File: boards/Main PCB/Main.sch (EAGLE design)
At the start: 87 parts, among them CN1 MINIB, CN2 MINIB, IC1 FT232RL, IC2 FT232RL, J1 3_PIN_JST-XH, J2 2_PIN_JST-XH, Q4 BSS138, Q5 BSS138, Q6 BSS138, Q7 BSS138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

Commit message: Fixed board to adhere to DRC's and fixed schematic to adhere to ERC's
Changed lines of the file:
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@@
 <part name="+3V9" library="supply1" library_urn="urn:adsk.eagle:library:371" deviceset="+3V3" device=""/>
 <part name="U4" library="TXS0104EDR" deviceset="TXS0104EDR" device=""/>
-<part name="+3V10" library="supply1" library_urn="urn:adsk.eagle:library:371" deviceset="+3V3" device=""/>
-<part name="P+6" library="supply1" library_urn="urn:adsk.eagle:library:371" deviceset="+5V" device=""/>
 <part name="GND32" library="supply1" library_urn="urn:adsk.eagle:library:371" deviceset="GND" device=""/>
 </parts>
@@
 <attribute name="NAME" x="431.35583125" y="94.6727" size="2.08746875" layer="95" ratio="10" rot="SMR180"/>
 <attribute name="VALUE" x="434.13266875" y="143.4777" size="2.08593125" layer="96" ratio="10" rot="SMR180"/>
-</instance>
-<instance part="+3V10" gate="G$1" x="411.48" y="104.14" smashed="yes">
-<attribute name="VALUE" x="408.94" y="99.06" size="1.778" layer="96" rot="R90"/>
-</instance>
-<instance part="P+6" gate="1" x="406.4" y="106.68" smashed="yes">
-<attribute name="VALUE" x="403.86" y="101.6" size="1.778" layer="96" rot="R90"/>
 </instance>
 <instance part="GND32" gate="1" x="414.02" y="132.08" smashed="yes">
@@
 <segment>
 <pinref part="U4" gate="A" pin="VCCA"/>
-<pinref part="+3V10" gate="G$1" pin="+3V3"/>
-<wire x1="419.1" y1="101.6" x2="411.48" y2="101.6" width="0.1524" layer="91"/>
+<wire x1="419.1" y1="101.6" x2="406.4" y2="101.6" width="0.1524" layer="91"/>
+<label x="406.4" y="101.6" size="1.778" layer="95" rot="R180"/>
 </segment>
 </net>
@@
 </segment>
 <segment>
+<pinref part="X1" gate="-5" pin="S"/>
+<label x="472.44" y="111.76" size="1.778" layer="95" rot="R90" xref="yes"/>
+<wire x1="472.44" y1="101.6" x2="472.44" y2="111.76" width="0.1524" layer="91"/>
+</segment>
+<segment>
 <pinref part="U4" gate="A" pin="VCCB"/>
-<pinref part="P+6" gate="1" pin="+5V"/>
 <wire x1="419.1" y1="104.14" x2="416.56" y2="104.14" width="0.1524" layer="91"/>
 <pinref part="U4" gate="A" pin="OE"/>
-<wire x1="416.56" y1="104.14" x2="406.4" y2="104.14" width="0.1524" layer="91"/>
+<wire x1="416.56" y1="104.14" x2="414.02" y2="104.14" width="0.1524" layer="91"/>
 <wire x1="419.1" y1="121.92" x2="416.56" y2="121.92" width="0.1524" layer="91"/>
 <wire x1="416.56" y1="121.92" x2="416.56" y2="104.14" width="0.1524" layer="91"/>
 <junction x="416.56" y="104.14"/>
-</segment>
-<segment>
-<pinref part="X1" gate="-5" pin="S"/>
-<label x="472.44" y="111.76" size="1.778" layer="95" rot="R90" xref="yes"/>
-<wire x1="472.44" y1="101.6" x2="472.44" y2="111.76" width="0.1524" layer="91"/>
+<label x="414.02" y="104.14" size="1.778" layer="95" rot="R180"/>
 </segment>
 </net>
@@
 <net name="N$46" class="0">
 <segment>
-<wire x1="114.3" y1="152.4" x2="114.3" y2="137.16" width="0.1524" layer="91"/>
+<wire x1="114.3" y1="144.78" x2="114.3" y2="137.16" width="0.1524" layer="91"/>
 <pinref part="U2" gate="G$1" pin="PA4/SPI1_NSS/TIM14_CH1/USART2_CK/USB_NOE/ADC_IN4"/>
 <wire x1="114.3" y1="137.16" x2="172.72" y2="137.16" width="0.1524" layer="91"/>
@@
 <pinref part="Q4" gate="G$1" pin="S"/>
 <wire x1="20.32" y1="154.94" x2="35.56" y2="154.94" width="0.1524" layer="91"/>
-<wire x1="114.3" y1="152.4" x2="35.56" y2="152.4" width="0.1524" layer="91"/>
-<wire x1="35.56" y1="152.4" x2="35.56" y2="154.94" width="0.1524" layer="91"/>
+<wire x1="114.3" y1="144.78" x2="35.56" y2="144.78" width="0.1524" layer="91"/>
+<wire x1="35.56" y1="144.78" x2="35.56" y2="154.94" width="0.1524" layer="91"/>
 <junction x="35.56" y="154.94"/>
 </segment>
@@
 <net name="N$50" class="0">
 <segment>
-<pinref part="Q8" gate="G$1" pin="S"/>
-<pinref part="R30" gate="G$1" pin="1"/>
-<wire x1="20.32" y1="203.2" x2="35.56" y2="203.2" width="0.1524" layer="91"/>
-<junction x="35.56" y="203.2"/>
-<wire x1="35.56" y1="203.2" x2="119.38" y2="203.2" width="0.1524" layer="91"/>
-<wire x1="119.38" y1="203.2" x2="119.38" y2="147.32" width="0.1524" layer="91"/>
+<wire x1="119.38" y1="182.88" x2="119.38" y2="147.32" width="0.1524" layer="91"/>
 <pinref part="U2" gate="G$1" pin="PA0/USART2_CTS/USART4_TX/RTC_TAMP2/WKUP1/ADC_IN0"/>
 <wire x1="119.38" y1="147.32" x2="172.72" y2="147.32" width="0.1524" layer="91"/>
-</segment>
-</net>
+<pinref part="R30" gate="G$1" pin="1"/>
+<pinref part="Q8" gate="G$1" pin="S"/>
+<wire x1="20.32" y1="203.2" x2="35.56" y2="203.2" width="0.1524" layer="91"/>
+<wire x1="119.38" y1="182.88" x2="35.56" y2="182.88" width="0.1524" layer="91"/>
+<wire x1="35.56" y1="182.88" x2="35.56" y2="203.2" width="0.1524" layer="91"/>
+<junction x="35.56" y="203.2"/>
+</segment>
+</net>

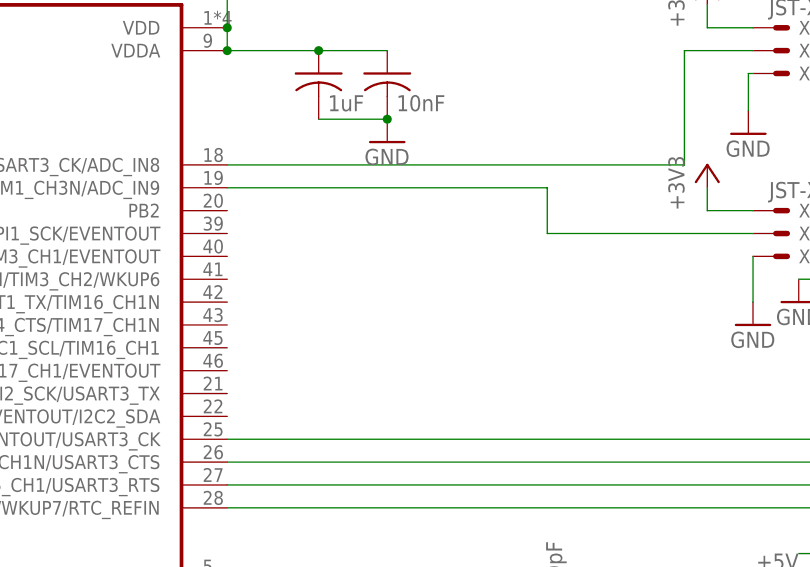
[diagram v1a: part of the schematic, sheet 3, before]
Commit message: Routed decoupling caps closer to micro and added vias for extra GPIO
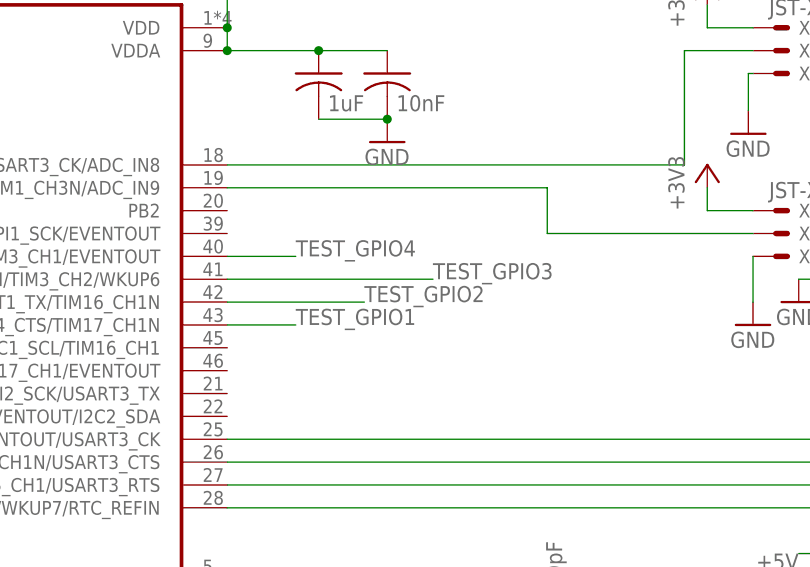
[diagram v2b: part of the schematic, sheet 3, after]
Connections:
- new net TEST_GPIO1: U2.PB7/I2C1_SDA/USART1_RX/USART4_CTS/TIM17_CH1N
- new net TEST_GPIO2: U2.PB6/I2C1_SCL/USART1_TX/TIM16_CH1N
- new net TEST_GPIO3: U2.PB5/SPI1_MOSI/I2C1_SMBA/TIM16_BKIN/TIM3_CH2/WKUP6
- new net TEST_GPIO4: U2.PB4/SPI1_MISO/TIM17_BKIN/TIM3_CH1/EVENTOUT
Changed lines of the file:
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@@
 <?xml version="1.0" encoding="utf-8"?>
 <!DOCTYPE eagle SYSTEM "eagle.dtd">
-<eagle version="9.2.2">
+<eagle version="9.3.0">
 <drawing>
 <settings>
@@
 </segment>
 </net>
+<net name="TEST_GPIO1" class="0">
+<segment>
+<pinref part="U2" gate="G$1" pin="PB7/I2C1_SDA/USART1_RX/USART4_CTS/TIM17_CH1N"/>
+<wire x1="350.52" y1="129.54" x2="358.14" y2="129.54" width="0.1524" layer="91"/>
+<label x="358.14" y="129.54" size="1.778" layer="95"/>
+</segment>
+</net>
+<net name="TEST_GPIO2" class="0">
+<segment>
+<pinref part="U2" gate="G$1" pin="PB6/I2C1_SCL/USART1_TX/TIM16_CH1N"/>
+<wire x1="350.52" y1="132.08" x2="365.76" y2="132.08" width="0.1524" layer="91"/>
+<label x="365.76" y="132.08" size="1.778" layer="95"/>
+</segment>
+</net>
+<net name="TEST_GPIO3" class="0">
+<segment>
+<pinref part="U2" gate="G$1" pin="PB5/SPI1_MOSI/I2C1_SMBA/TIM16_BKIN/TIM3_CH2/WKUP6"/>
+<wire x1="350.52" y1="134.62" x2="373.38" y2="134.62" width="0.1524" layer="91"/>
+<label x="373.38" y="134.62" size="1.778" layer="95"/>
+</segment>
+</net>
+<net name="TEST_GPIO4" class="0">
+<segment>
+<pinref part="U2" gate="G$1" pin="PB4/SPI1_MISO/TIM17_BKIN/TIM3_CH1/EVENTOUT"/>
+<wire x1="350.52" y1="137.16" x2="358.14" y2="137.16" width="0.1524" layer="91"/>
+<label x="358.14" y="137.16" size="1.778" layer="95"/>
+</segment>
+</net>

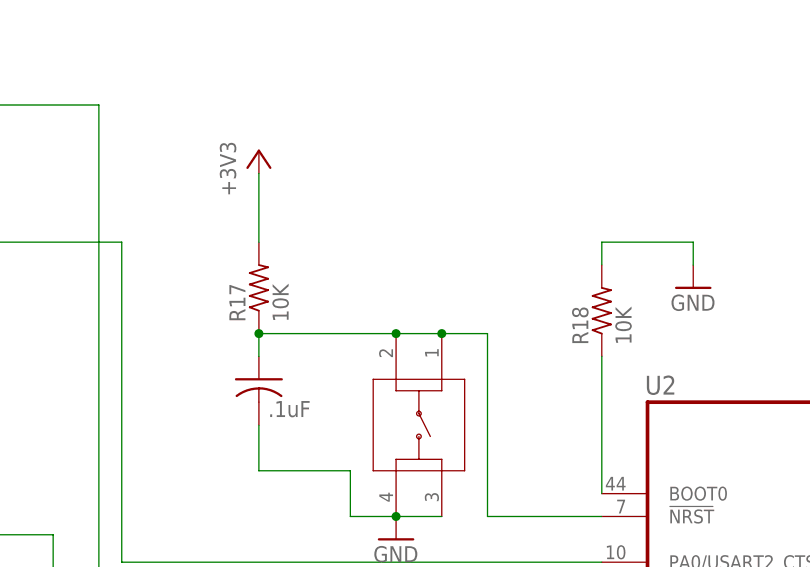
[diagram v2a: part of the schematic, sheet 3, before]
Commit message: Fixing board routing and adding reset pin per Todd's suggestions
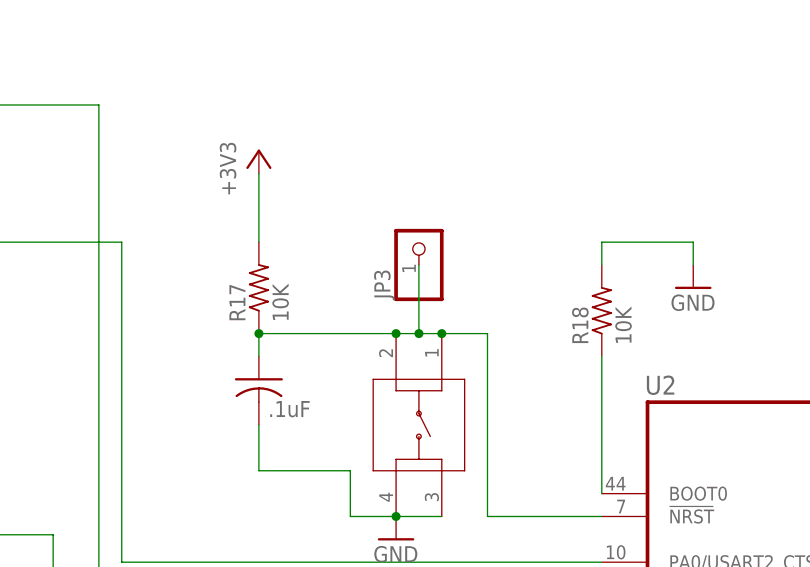
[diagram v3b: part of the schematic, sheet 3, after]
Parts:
- added JP3: (no value), pinhead:PINHD-1X1
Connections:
- net N$43: now also JP3.1
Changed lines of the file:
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@@
 <part name="U4" library="TXS0104EDR" deviceset="TXS0104EDR" device=""/>
 <part name="GND32" library="supply1" library_urn="urn:adsk.eagle:library:371" deviceset="GND" device=""/>
+<part name="JP3" library="pinhead" library_urn="urn:adsk.eagle:library:325" deviceset="PINHD-1X1" device="" package3d_urn="urn:adsk.eagle:package:22485/2"/>
 </parts>
 <sheets>
@@
 <instance part="GND32" gate="1" x="414.02" y="132.08" smashed="yes">
 <attribute name="VALUE" x="411.48" y="129.54" size="1.778" layer="96"/>
+</instance>
+<instance part="JP3" gate="G$1" x="152.4" y="182.88" smashed="yes" rot="R90">
+<attribute name="NAME" x="149.225" y="176.53" size="1.778" layer="95" rot="R90"/>
+<attribute name="VALUE" x="157.48" y="176.53" size="1.778" layer="96" rot="R90"/>
 </instance>
 </instances>
@@
 <junction x="134.62" y="172.72"/>
 <pinref part="RESET" gate="G$1" pin="1"/>
-<wire x1="149.86" y1="172.72" x2="154.94" y2="172.72" width="0.1524" layer="91"/>
+<wire x1="149.86" y1="172.72" x2="152.4" y2="172.72" width="0.1524" layer="91"/>
 <junction x="149.86" y="172.72"/>
+<wire x1="152.4" y1="172.72" x2="154.94" y2="172.72" width="0.1524" layer="91"/>
 <wire x1="160.02" y1="172.72" x2="154.94" y2="172.72" width="0.1524" layer="91"/>
 <junction x="154.94" y="172.72"/>
-</segment>
-</net>
+<pinref part="JP3" gate="G$1" pin="1"/>
+<wire x1="152.4" y1="180.34" x2="152.4" y2="172.72" width="0.1524" layer="91"/>
+<junction x="152.4" y="172.72"/>
+</segment>
+</net>

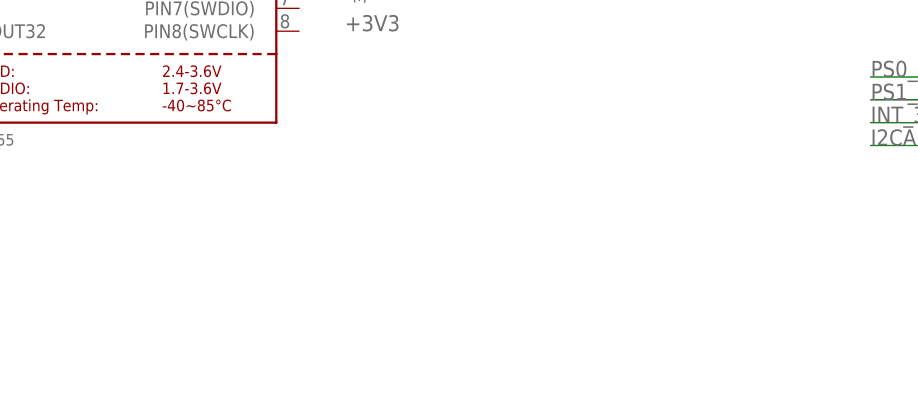
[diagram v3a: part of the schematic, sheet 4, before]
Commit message: Routed headers for IMU backup
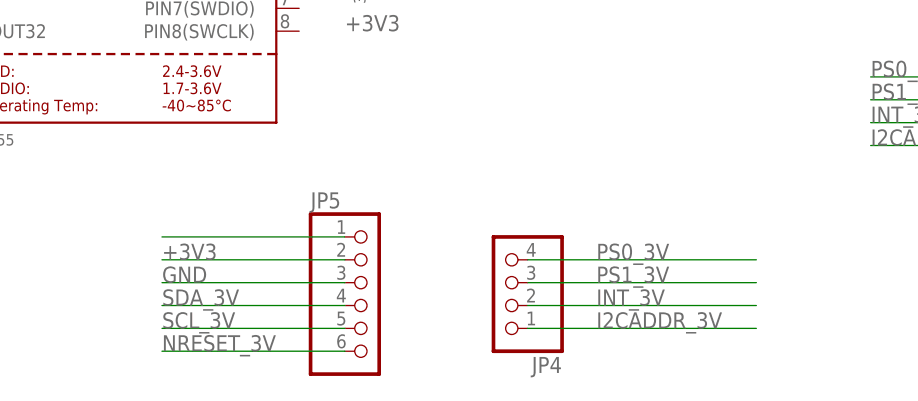
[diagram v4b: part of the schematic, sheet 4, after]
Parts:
- added JP4: (no value), microbuilder:HEADER-1X476MIL
- added JP5: (no value), main_library:MICROBUILDER_HEADER-1X676MIL
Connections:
- new net N$59: JP5.1
- net +3V3: now also JP5.2
- net GND: now also JP5.3
- net I2CADDR_3V: now also JP4.1
- net INT_3V: now also JP4.2
- net NRESET_3V: now also JP5.6
- net PS0_3V: now also JP4.4
- net PS1_3V: now also JP4.3
- net SCL_3V: now also JP5.5
- net SDA_3V: now also JP5.4
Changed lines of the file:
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@@
 <part name="GND32" library="supply1" library_urn="urn:adsk.eagle:library:371" deviceset="GND" device=""/>
 <part name="JP3" library="pinhead" library_urn="urn:adsk.eagle:library:325" deviceset="PINHD-1X1" device="" package3d_urn="urn:adsk.eagle:package:22485/2"/>
+<part name="JP4" library="microbuilder" deviceset="HEADER-1X4" device="76MIL"/>
+<part name="JP5" library="main_library" deviceset="MICROBUILDER_HEADER-1X6" device="76MIL"/>
 </parts>
 <sheets>
@@
 <attribute name="DRAWING_NAME" x="63.5" y="-105.41" size="2.54" layer="94"/>
 </instance>
+<instance part="JP4" gate="A" x="-7.62" y="-58.42" smashed="yes" rot="R180">
+<attribute name="NAME" x="-1.27" y="-66.675" size="1.778" layer="95" rot="R180"/>
+<attribute name="VALUE" x="-1.27" y="-50.8" size="1.778" layer="96" rot="R180"/>
+</instance>
+<instance part="JP5" gate="A" x="-22.86" y="-60.96" smashed="yes">
+<attribute name="NAME" x="-29.21" y="-50.165" size="1.778" layer="95"/>
+<attribute name="VALUE" x="-29.21" y="-71.12" size="1.778" layer="96"/>
+</instance>
 </instances>
 <busses>
@@
 <wire x1="7.62" y1="-20.32" x2="10.16" y2="-20.32" width="0.1524" layer="91"/>
 </segment>
+<segment>
+<pinref part="JP5" gate="A" pin="3"/>
+<wire x1="-25.4" y1="-58.42" x2="-45.72" y2="-58.42" width="0.1524" layer="91"/>
+<label x="-45.72" y="-58.42" size="1.778" layer="95"/>
+</segment>
 </net>
 <net name="SDA_3V" class="0">
@@
 <label x="-27.94" y="5.08" size="1.778" layer="95"/>
 </segment>
+<segment>
+<pinref part="JP5" gate="A" pin="4"/>
+<wire x1="-25.4" y1="-60.96" x2="-45.72" y2="-60.96" width="0.1524" layer="91"/>
+<label x="-45.72" y="-60.96" size="1.778" layer="95"/>
+</segment>
 </net>
 <net name="SCL_3V" class="0">
@@
 <wire x1="-30.48" y1="2.54" x2="-17.78" y2="2.54" width="0.1524" layer="91"/>
 <label x="-27.94" y="2.54" size="1.778" layer="95"/>
+</segment>
+<segment>
+<pinref part="JP5" gate="A" pin="5"/>
+<wire x1="-25.4" y1="-63.5" x2="-45.72" y2="-63.5" width="0.1524" layer="91"/>
+<label x="-45.72" y="-63.5" size="1.778" layer="95"/>
 </segment>
 </net>
@@
 <pinref part="JP2" gate="A" pin="2"/>
 </segment>
+<segment>
+<pinref part="JP4" gate="A" pin="3"/>
+<wire x1="-5.08" y1="-58.42" x2="20.32" y2="-58.42" width="0.1524" layer="91"/>
+<label x="2.54" y="-58.42" size="1.778" layer="95"/>
+</segment>
 </net>
 <net name="PS0_3V" class="0">
@@
 <pinref part="JP2" gate="A" pin="1"/>
 </segment>
+<segment>
+<pinref part="JP4" gate="A" pin="4"/>
+<wire x1="-5.08" y1="-55.88" x2="20.32" y2="-55.88" width="0.1524" layer="91"/>
+<label x="2.54" y="-55.88" size="1.778" layer="95"/>
+</segment>
 </net>
 <net name="NRESET_3V" class="0">
@@
 <label x="-27.94" y="-12.7" size="1.778" layer="95"/>
 </segment>
+<segment>
+<pinref part="JP5" gate="A" pin="6"/>
+<wire x1="-25.4" y1="-66.04" x2="-45.72" y2="-66.04" width="0.1524" layer="91"/>
+<label x="-45.72" y="-66.04" size="1.778" layer="95"/>
+</segment>
 </net>
 <net name="INT_3V" class="0">
@@
 <label x="33.02" y="-40.64" size="1.778" layer="95"/>
 <pinref part="JP2" gate="A" pin="3"/>
+</segment>
+<segment>
+<pinref part="JP4" gate="A" pin="2"/>
+<wire x1="-5.08" y1="-60.96" x2="20.32" y2="-60.96" width="0.1524" layer="91"/>
+<label x="2.54" y="-60.96" size="1.778" layer="95"/>
 </segment>
 </net>
@@
 <label x="33.02" y="-43.18" size="1.778" layer="95"/>
 <pinref part="JP2" gate="A" pin="4"/>
+</segment>
+<segment>
+<pinref part="JP4" gate="A" pin="1"/>
+<wire x1="-5.08" y1="-63.5" x2="20.32" y2="-63.5" width="0.1524" layer="91"/>
+<label x="2.54" y="-63.5" size="1.778" layer="95"/>
 </segment>
 </net>
@@
 <label x="-76.2" y="5.08" size="1.778" layer="95"/>
 </segment>
-</net>
+<segment>
+<pinref part="JP5" gate="A" pin="2"/>
+<wire x1="-25.4" y1="-55.88" x2="-45.72" y2="-55.88" width="0.1524" layer="91"/>
+<label x="-45.72" y="-55.88" size="1.778" layer="95"/>
+</segment>
+</net>
+<net name="N$59" class="0">
+<segment>
+<pinref part="JP5" gate="A" pin="1"/>
+<wire x1="-25.4" y1="-53.34" x2="-45.72" y2="-53.34" width="0.1524" layer="91"/>
+</segment>
+</net>
